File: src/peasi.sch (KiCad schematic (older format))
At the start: 13 parts

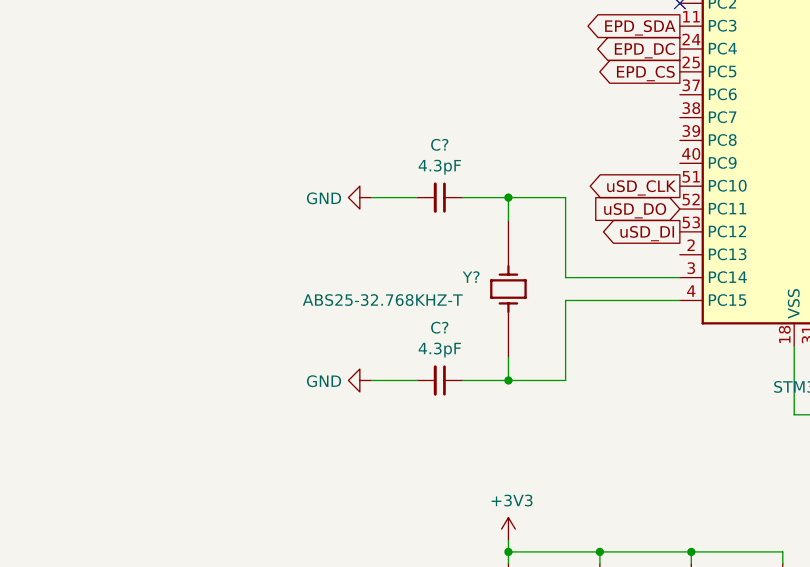
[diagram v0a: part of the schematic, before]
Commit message: fix libraries on macos
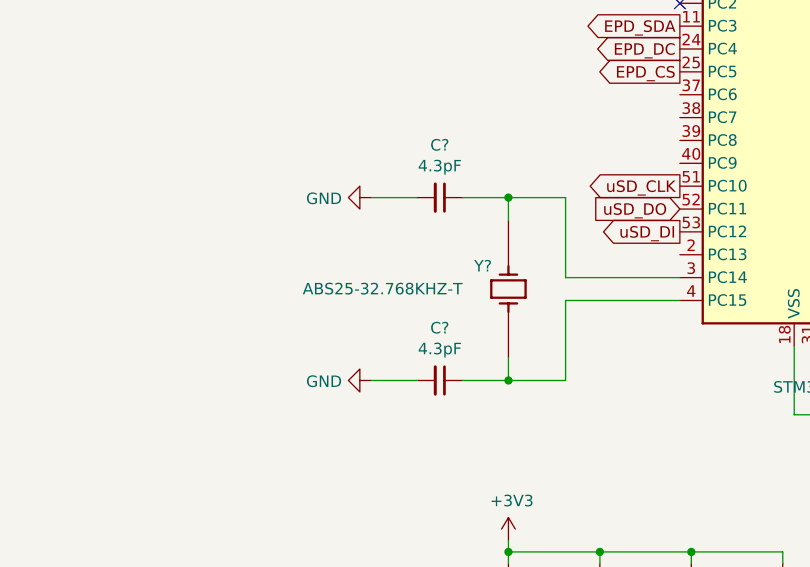
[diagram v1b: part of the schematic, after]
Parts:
- removed Y?: ABS25-32.768KHZ-T, XTAL_ABS25-32.768KHZ-6-1-T, symbol ABS25-32.768KHZ-T:ABS25-32.768KHZ-T
- added Y?: ABS25-32.768KHZ-T, XTAL_ABS25-32.768KHZ-6-1-T, symbol ABS25-32.768KHZ-T:ABS25-32.768KHZ-T
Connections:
- net at C?.1, U?.3 (PC14): now also Y?.1
- net at C?.1, U?.4 (PC15): now also Y?.4
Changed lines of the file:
@@
-$EndComp
-$Comp
-L ABS25-32.768KHZ-T:ABS25-32.768KHZ-T Y?
-U 1 1 61761BB9
-P 4550 5550
-F 0 "Y?" V 4500 5350 50  0000 L CNN
-F 1 "ABS25-32.768KHZ-T" V 4600 4650 50  0000 L CNN
-F 2 "XTAL_ABS25-32.768KHZ-6-1-T" H 4550 5550 50  0001 L BNN
-F 3 "" H 4550 5550 50  0001 L BNN
-F 4 "12.01.15" H 4550 5550 50  0001 L BNN "PARTREV"
-F 5 "Abracon Corporation" H 4550 5550 50  0001 L BNN "MANUFACTURER"
-F 6 "Manufacturer Recommendations" H 4550 5550 50  0001 L BNN "STANDARD"
-	1    4550 5550
-	0    1    1    0
 $EndComp
 $Comp
@@
 Text GLabel 7500 3500 2    50   BiDi ~ 0
 D+
+$Comp
+L ABS25-32.768KHZ-T:ABS25-32.768KHZ-T Y?
+U 1 1 617AD663
+P 4550 5550
+F 0 "Y?" V 4450 5400 50  0000 L CNN
+F 1 "ABS25-32.768KHZ-T" V 4550 4650 50  0000 L CNN
+F 2 "XTAL_ABS25-32.768KHZ-6-1-T" H 4550 5550 50  0001 L BNN
+F 3 "" H 4550 5550 50  0001 L BNN
+F 4 "12.01.15" H 4550 5550 50  0001 L BNN "PARTREV"
+F 5 "Abracon Corporation" H 4550 5550 50  0001 L BNN "MANUFACTURER"
+F 6 "Manufacturer Recommendations" H 4550 5550 50  0001 L BNN "STANDARD"
+	1    4550 5550
+	0    1    1    0
+$EndComp
 $EndSCHEMATC

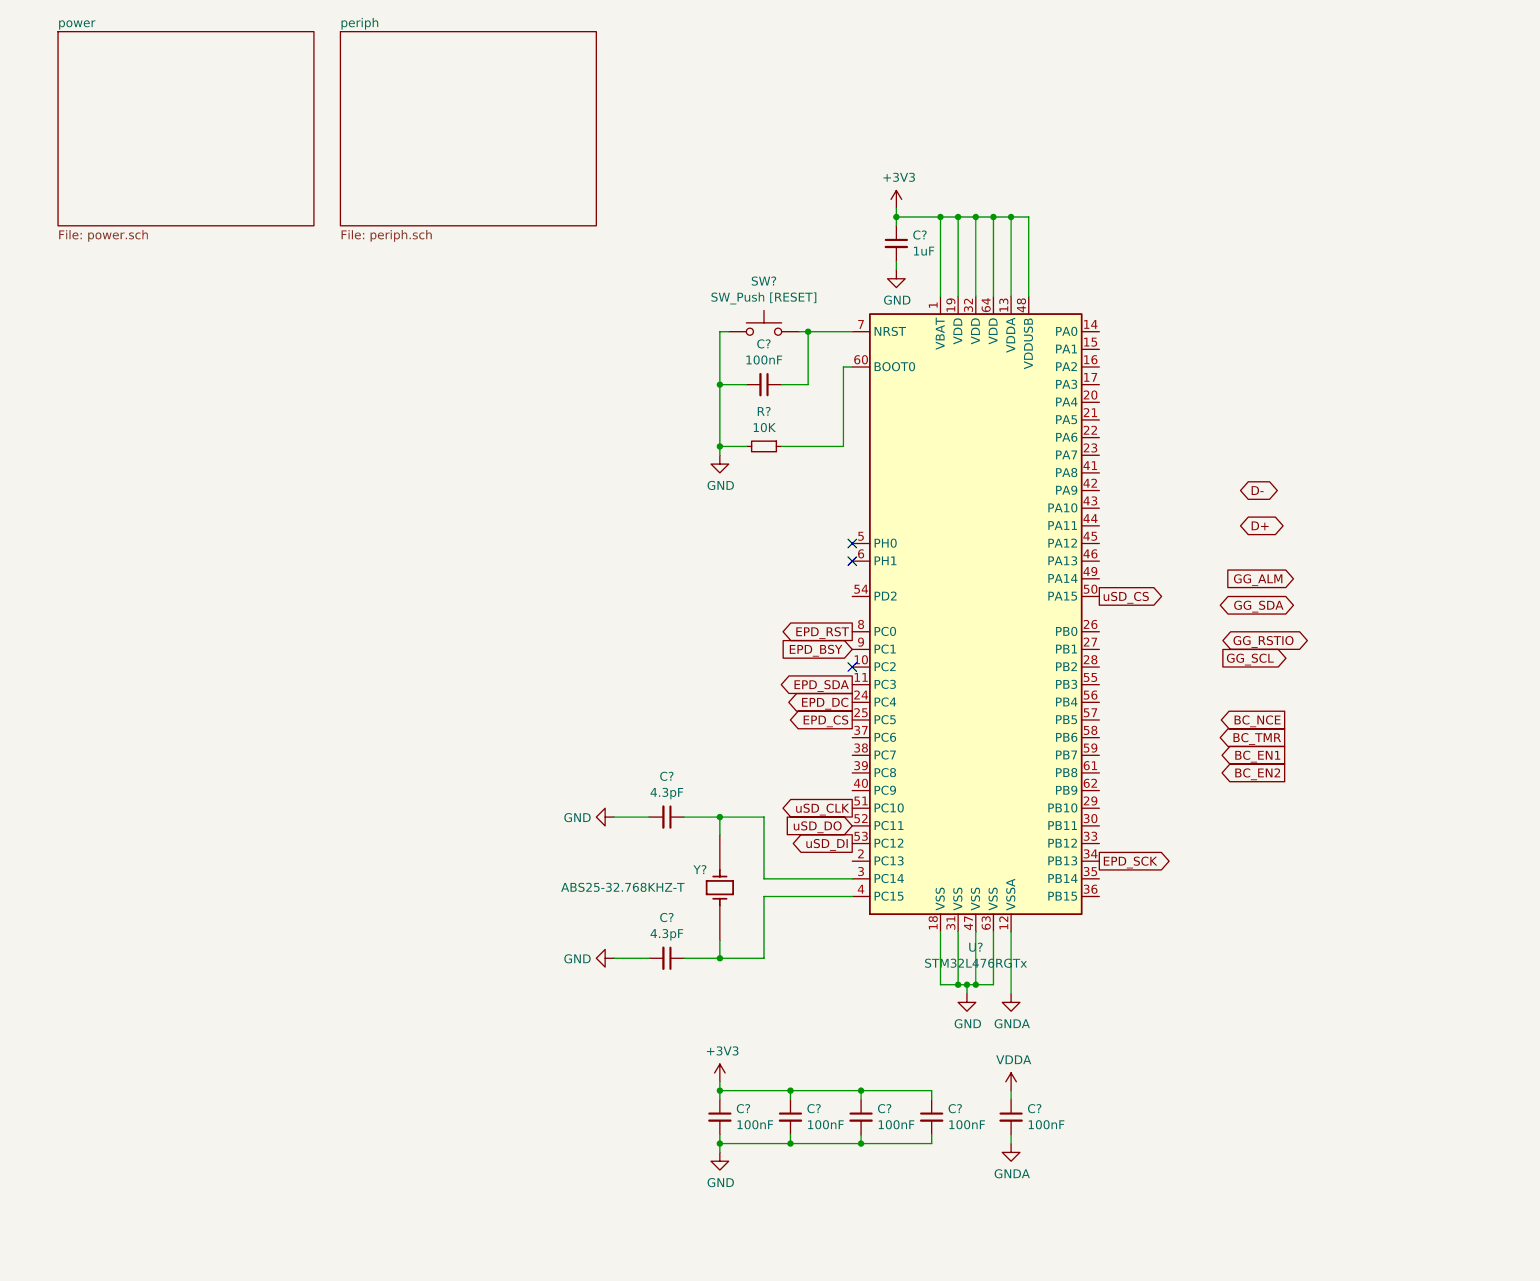
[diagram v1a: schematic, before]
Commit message: switch MCU to STM32G0-series
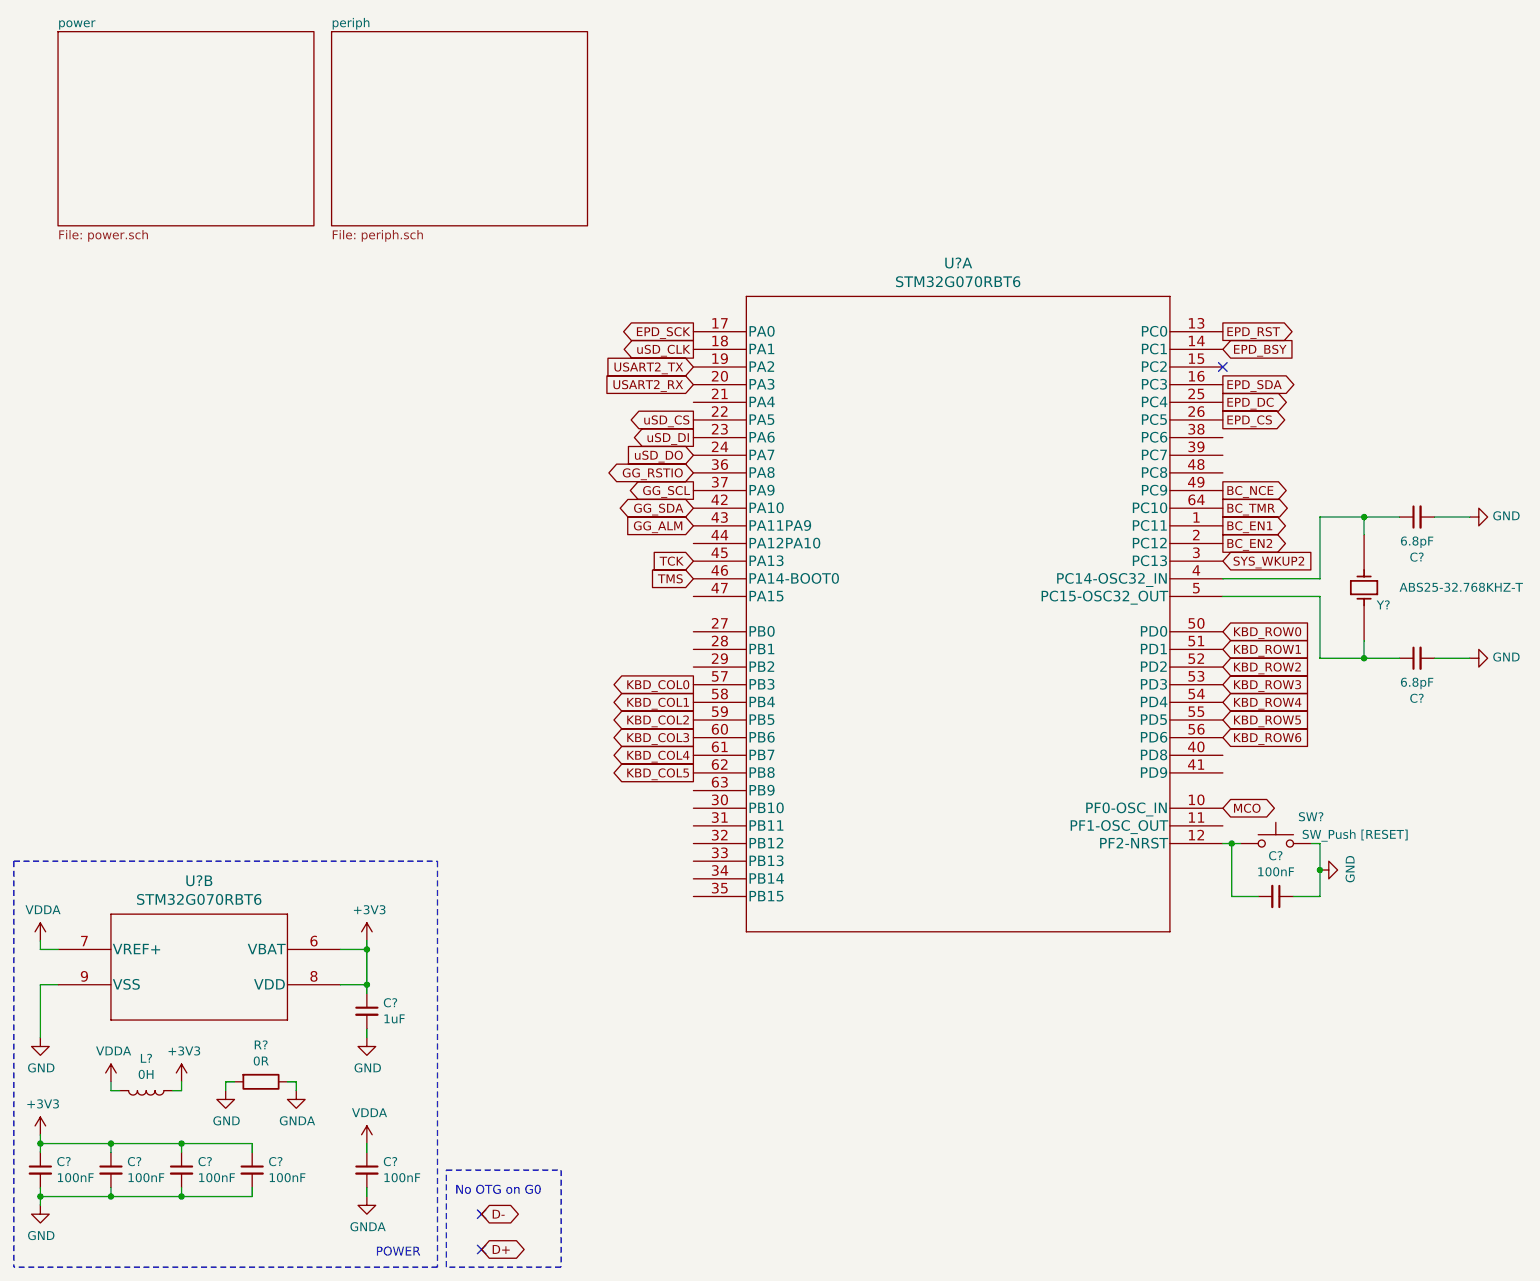
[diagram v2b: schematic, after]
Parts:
- removed R?: 10K, symbol Device:R_Small
- removed U?: STM32L476RGTx, Package_QFP:LQFP-64_10x10mm_P0.5mm, symbol MCU_ST_STM32L4:STM32L476RGTx
- added L?: 0H, symbol Device:L
- added R?: 0R, symbol Device:R
- added U? (x2): STM32G070RBT6, LQFP-64, symbol STM32G070RBT6:STM32G070RBT6
- C? (x2): value 4.3pF -> 6.8pF
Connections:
- net +3V3: now also L?.1, U?.6 (VBAT), U?.8 (VDD)
- net BC_EN1: now also U?.1 (PC11)
- net BC_EN2: now also U?.2 (PC12)
- net BC_NCE: now also U?.49 (PC9)
- net BC_TMR: now also U?.64 (PC10)
- net EPD_BSY: now also U?.14 (PC1)
- net EPD_CS: now also U?.26 (PC5)
- net EPD_DC: now also U?.25 (PC4)
- net EPD_RST: now also U?.13 (PC0)
- net EPD_SCK: now also U?.17 (PA0)
- net EPD_SDA: now also U?.16 (PC3)
- net GG_ALM: now also U?.43 (PA11PA9)
- net GG_RSTIO: now also U?.36 (PA8)
- net GG_SCL: now also U?.37 (PA9)
- net GG_SDA: now also U?.42 (PA10)
- net GND: now also C?.1, SW?.2, R?.2, U?.9 (VSS); no longer C?.2, SW?.1
- net GNDA: now also R?.1
- net VDDA: now also L?.2, U?.7 (VREF+)
- net uSD_CLK: now also U?.18 (PA1)
- net uSD_CS: now also U?.22 (PA5)
- net uSD_DI: now also U?.23 (PA6)
- net uSD_DO: now also U?.24 (PA7)
- net at C?.1, Y?.1: now also U?.5 (PC15-OSC32_OUT)
- net at C?.1, Y?.4: now also U?.4 (PC14-OSC32_IN)
- new net: C?.2, SW?.1, U?.12 (PF2-NRST)
- new net KBD_COL0: U?.57 (PB3)
- new net KBD_COL1: U?.58 (PB4)
- new net KBD_COL2: U?.59 (PB5)
- new net KBD_COL3: U?.60 (PB6)
- new net KBD_COL4: U?.61 (PB7)
- new net KBD_COL5: U?.62 (PB8)
- new net KBD_ROW0: U?.50 (PD0)
- new net KBD_ROW1: U?.51 (PD1)
- new net KBD_ROW2: U?.52 (PD2)
- new net KBD_ROW3: U?.53 (PD3)
- new net KBD_ROW4: U?.54 (PD4)
- new net KBD_ROW5: U?.55 (PD5)
- new net KBD_ROW6: U?.56 (PD6)
- new net MCO: U?.10 (PF0-OSC_IN)
- new net SYS_WKUP2: U?.3 (PC13)
- new net TCK: U?.45 (PA13)
- new net TMS: U?.46 (PA14-BOOT0)
- new net USART2_RX: U?.20 (PA3)
- new net USART2_TX: U?.19 (PA2)
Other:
- note added: "No OTG on G0"
- note added: "POWER"
- moved on the sheet: C?, SW?, Y?
